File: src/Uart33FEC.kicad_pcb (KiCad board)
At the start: 2 copper layers, 24 x 27.9 mm, 28 parts, among them J1 105444-0001, J2 B4B-XH-A, Q1 DMP3099L-13, U1 FT230XS, U2 MIC2005A-1

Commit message: Changed pinout to GND RXD TXD 3V3
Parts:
- moved D1 1.31 mm to (32.0, 39.2)
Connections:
- J2 pad 1: RX -> GND
- J2 pad 2: GND -> RX
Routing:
- net GND: track 110.2 -> 112.3 mm
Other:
- board text added: "Uart33FEC BXXXX"
- board text removed: "Uart33FEC AXXXX"
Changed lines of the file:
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@@
 			(chamfer_ratio 0.2)
 			(chamfer top_left bottom_left)
-			(net 17 "RX")
+			(net 1 "GND")
 		)
 		(pad "2" smd roundrect
@@
 			(layers "F.Cu" "F.Paste" "F.Mask")
 			(roundrect_rratio 0.25)
-			(net 1 "GND")
+			(net 17 "RX")
 		)
 		(pad "3" smd roundrect
@@
 		)
 		(property "Value" "10uF"
-			(at 0 1.7 0)
+			(at 1 1.6 0)
 			(layer "B.SilkS")
 			(effects
@@
 	(footprint "Medo64:D TVS SM05T1G (SOT23-3)"
 		(layer "B.Cu")
-		(at 30.75 39.6 180)
+		(at 32 39.2 180)
 		(descr "SM05T1G [SM05T1GOSCT-ND]")
 		(property "Reference" "D1"
-			(at -2.25 0 0)
+			(at 0 -1 0)
 			(layer "B.SilkS")
 			(effects
@@
 	)
 	(gr_text "RX"
-		(at 28.25 38.7 0)
+		(at 30.8 38.7 0)
 		(layer "F.SilkS" knockout)
 		(effects
@@
 	)
 	(gr_text "TX"
-		(at 33.2 38.7 0)
+		(at 33.1 38.7 0)
 		(layer "F.SilkS" knockout)
 		(effects
@@
 		)
 	)
-	(gr_text "Uart33FEC AXXXX"
+	(gr_text "Uart33FEC BXXXX"
 		(at 21 33 90)
 		(layer "F.SilkS")
@@
 	)
 	(gr_text "GND"
-		(at 30.75 38.7 0)
+		(at 28.1 38.7 0)
 		(layer "F.SilkS" knockout)
 		(effects
@@
 	)
 	(segment
+		(start 28.25 40.8)
+		(end 28.25 38.8)
+		(width 0.35)
+		(layer "F.Cu")
+		(net 1)
+	)
+	(segment
 		(start 33.6325 30.6825)
 		(end 34.7 30.6825)
@@
 	)
 	(via
-		(at 30.75 40.8)
+		(at 29.4 23.2)
 		(size 0.6)
 		(drill 0.3)
@@
 	)
 	(via
-		(at 29.4 23.2)
+		(at 28.25 38.8)
 		(size 0.6)
 		(drill 0.3)
@@
 	)
 	(segment
-		(start 30.75 38.85)
-		(end 30.75 40.8)
-		(width 0.35)
-		(layer "B.Cu")
-		(net 1)
-	)
-	(segment
 		(start 36.4 30.25)
 		(end 34.9 30.25)
@@
 	)
 	(segment
-		(start 30.75 37.6)
-		(end 28.75 37.6)
+		(start 28.25 38.275)
+		(end 28.3 38.225)
 		(width 0.35)
 		(layer "B.Cu")
@@
 	)
 	(segment
-		(start 30.75 37.9)
-		(end 30.75 37.6)
+		(start 27.925 38.225)
+		(end 27.5 37.8)
 		(width 0.35)
 		(layer "B.Cu")
@@
 	)
 	(segment
-		(start 30.75 38.625)
-		(end 30.75 37.9)
+		(start 33.075 38.225)
+		(end 33.4 37.9)
 		(width 0.35)
 		(layer "B.Cu")
@@
 	)
 	(segment
-		(start 30.75 37.6)
-		(end 32.1 37.6)
+		(start 33.9 33.3)
+		(end 33.9 35.05)
 		(width 0.35)
 		(layer "B.Cu")
@@
 	)
 	(segment
-		(start 33.9 33.3)
-		(end 33.9 35.05)
+		(start 37.8 35.05)
+		(end 36.7 35.05)
 		(width 0.35)
 		(layer "B.Cu")
@@
 	)
 	(segment
-		(start 37.8 35.05)
-		(end 36.7 35.05)
+		(start 33.4 37.9)
+		(end 33.4 36.3)
 		(width 0.35)
 		(layer "B.Cu")
@@
 	)
 	(segment
+		(start 27.5 36.2)
+		(end 27.5 37.8)
+		(width 0.35)
+		(layer "B.Cu")
+		(net 1)
+	)
+	(segment
 		(start 30.05 23.85)
 		(end 33.95 23.85)
@@
 	)
 	(segment
-		(start 28.75 37.6)
-		(end 27.5 36.35)
-		(width 0.35)
-		(layer "B.Cu")
-		(net 1)
-	)
-	(segment
 		(start 29.25 23.05)
 		(end 29.25 22.1)
@@
 	)
 	(segment
+		(start 32 38.225)
+		(end 28.3 38.225)
+		(width 0.35)
+		(layer "B.Cu")
+		(net 1)
+	)
+	(segment
 		(start 33.9 35.05)
 		(end 33.9 35.7)
@@
 	)
 	(segment
+		(start 28.25 38.8)
+		(end 28.25 38.275)
+		(width 0.35)
+		(layer "B.Cu")
+		(net 1)
+	)
+	(segment
 		(start 36.7 35.05)
 		(end 36.7 34.75)
@@
 	)
 	(segment
+		(start 28.3 38.225)
+		(end 27.925 38.225)
+		(width 0.35)
+		(layer "B.Cu")
+		(net 1)
+	)
+	(segment
 		(start 29.4 23.2)
 		(end 29.25 23.05)
@@
 	)
 	(segment
-		(start 32.1 37.6)
-		(end 33.4 36.3)
-		(width 0.35)
-		(layer "B.Cu")
-		(net 1)
-	)
-	(segment
 		(start 33.9 35.7)
 		(end 33.4 36.2)
@@
 	)
 	(segment
+		(start 32 38.225)
+		(end 33.075 38.225)
+		(width 0.35)
+		(layer "B.Cu")
+		(net 1)
+	)
+	(segment
 		(start 31.25 23.65)
 		(end 30.7 24.2)
@@
 	)
 	(segment
-		(start 29.3 37.9)
-		(end 26.5 37.9)
-		(width 0.2)
-		(layer "F.Cu")
-		(net 9)
-	)
-	(segment
-		(start 26.5 37.9)
-		(end 24.55 39.85)
+		(start 24.55 39.85)
+		(end 24.55 42.65)
 		(width 0.2)
 		(layer "F.Cu")
@@
 	)
 	(segment
-		(start 24.55 39.85)
-		(end 24.55 42.65)
-		(width 0.2)
-		(layer "F.Cu")
-		(net 9)
-	)
-	(segment
 		(start 39.45 37.9)
 		(end 29.3 37.9)
@@
 	)
 	(segment
+		(start 26.5 37.9)
+		(end 24.55 39.85)
+		(width 0.2)
+		(layer "F.Cu")
+		(net 9)
+	)
+	(segment
 		(start 42.5 35.7)
 		(end 42.5 31.3)
@@
 		(net 9)
 	)
+	(segment
+		(start 29.3 37.9)
+		(end 26.5 37.9)
+		(width 0.2)
+		(layer "F.Cu")
+		(net 9)
+	)
 	(via
 		(at 24.55 42.65)
@@
 	)
 	(segment
-		(start 29.199944 40.8)
-		(end 29.2 40.800056)
-		(width 0.2)
-		(layer "F.Cu")
-		(net 17)
-	)
-	(segment
-		(start 28.25 40.8)
-		(end 29.199944 40.8)
-		(width 0.35)
-		(layer "F.Cu")
-		(net 17)
-	)
-	(segment
 		(start 29.2825 30.7)
 		(end 26.1 30.7)
@@
 	)
 	(via
-		(at 29.2 40.800056)
+		(at 30.75 40.8)
 		(size 0.6)
 		(drill 0.3)
@@
 	)
 	(segment
-		(start 29.2 40.800056)
-		(end 29.799944 40.800056)
+		(start 26.05 38.25)
+		(end 26.05 30.65)
 		(width 0.35)
 		(layer "B.Cu")
@@
 	)
 	(segment
-		(start 29.8 40.574998)
-		(end 25.65 36.424998)
+		(start 28.6 40.8)
+		(end 26.05 38.25)
 		(width 0.35)
 		(layer "B.Cu")
@@
 	)
 	(segment
-		(start 25.65 31.05)
-		(end 26.05 30.65)
+		(start 30.75 40.8)
+		(end 28.6 40.8)
 		(width 0.35)
 		(layer "B.Cu")
@@
 	)
 	(segment
-		(start 25.65 36.424998)
-		(end 25.65 31.05)
+		(start 30.75 40.8)
+		(end 30.749944 40.800056)
 		(width 0.35)
 		(layer "B.Cu")
@@
 	(segment
 		(start 33.25 40.8)
-		(end 32.3 40.8)
+		(end 33.250022 40.8)
 		(width 0.35)
 		(layer "F.Cu")
@@
 	)
 	(via
-		(at 32.3 40.8)
+		(at 33.250022 40.8)
 		(size 0.6)
 		(drill 0.3)
@@
 	)
 	(segment
-		(start 24.35 38.05)
-		(end 24.35 30.1)
+		(start 31.850022 42.2)
+		(end 33.250022 40.8)
 		(width 0.35)
 		(layer "B.Cu")
@@
 	)
 	(segment
-		(start 30.8 42.25)
-		(end 28.55 42.25)
+		(start 25.63932 28.76068)
+		(end 24.35 30.05)
 		(width 0.35)
 		(layer "B.Cu")
@@
 	)
 	(segment
-		(start 31.7 41.35)
-		(end 30.8 42.25)
+		(start 24.35 38.85)
+		(end 27.7 42.2)
 		(width 0.35)
 		(layer "B.Cu")
@@
 	)
 	(segment
-		(start 28.55 42.25)
-		(end 24.35 38.05)
+		(start 26.050002 28.76068)
+		(end 25.63932 28.76068)
 		(width 0.35)
 		(layer "B.Cu")
@@
 	)
 	(segment
-		(start 31.7 40.575)
-		(end 31.7 41.35)
+		(start 27.7 42.2)
+		(end 31.850022 42.2)
 		(width 0.35)
 		(layer "B.Cu")
@@
 	)
 	(segment
-		(start 31.925 40.8)
-		(end 31.7 40.575)
-		(width 0.35)
-		(layer "B.Cu")
-		(net 18)
-	)
-	(segment
-		(start 32.3 40.8)
-		(end 31.925 40.8)
-		(width 0.35)
-		(layer "B.Cu")
-		(net 18)
-	)
-	(segment
-		(start 24.35 30.1)
-		(end 25.68932 28.76068)
-		(width 0.35)
-		(layer "B.Cu")
-		(net 18)
-	)
-	(segment
-		(start 25.68932 28.76068)
-		(end 26.050002 28.76068)
+		(start 24.35 30.05)
+		(end 24.35 38.85)
 		(width 0.35)
 		(layer "B.Cu")

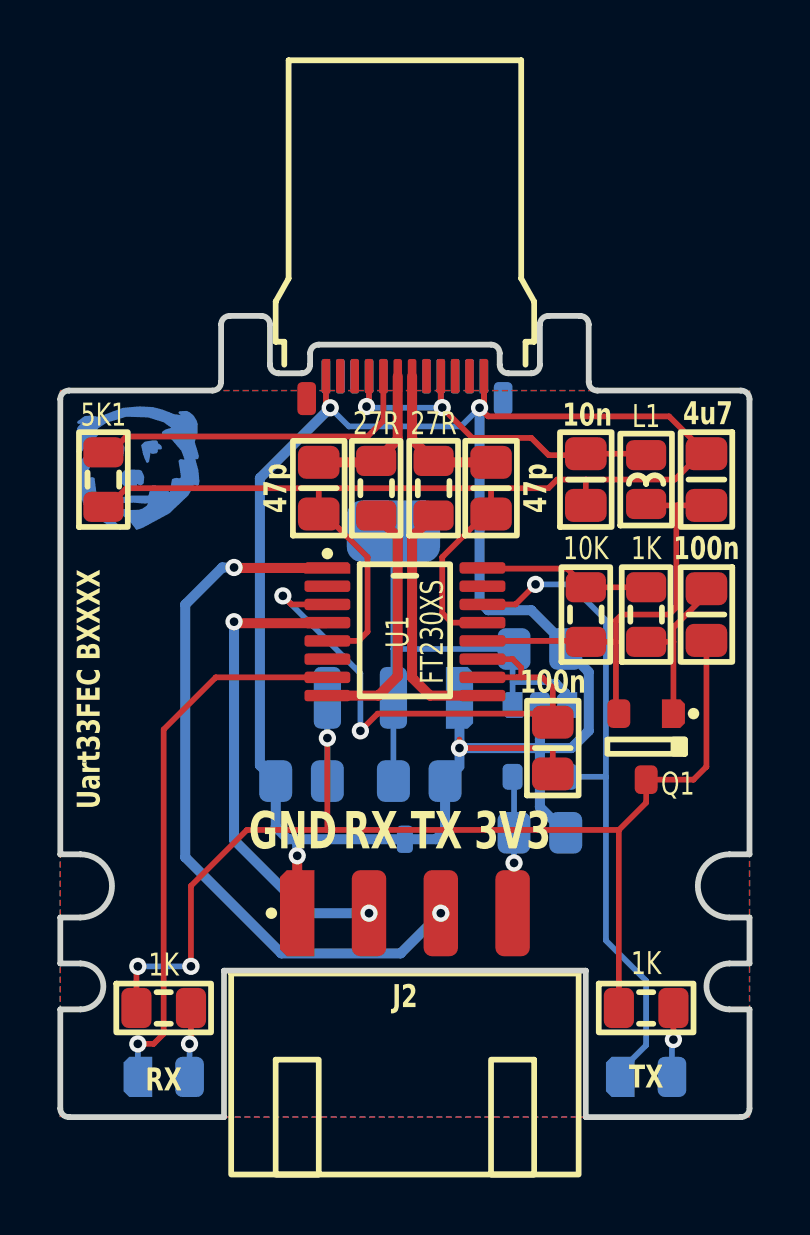
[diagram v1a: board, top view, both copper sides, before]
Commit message: Changed load switch (400mA limit)
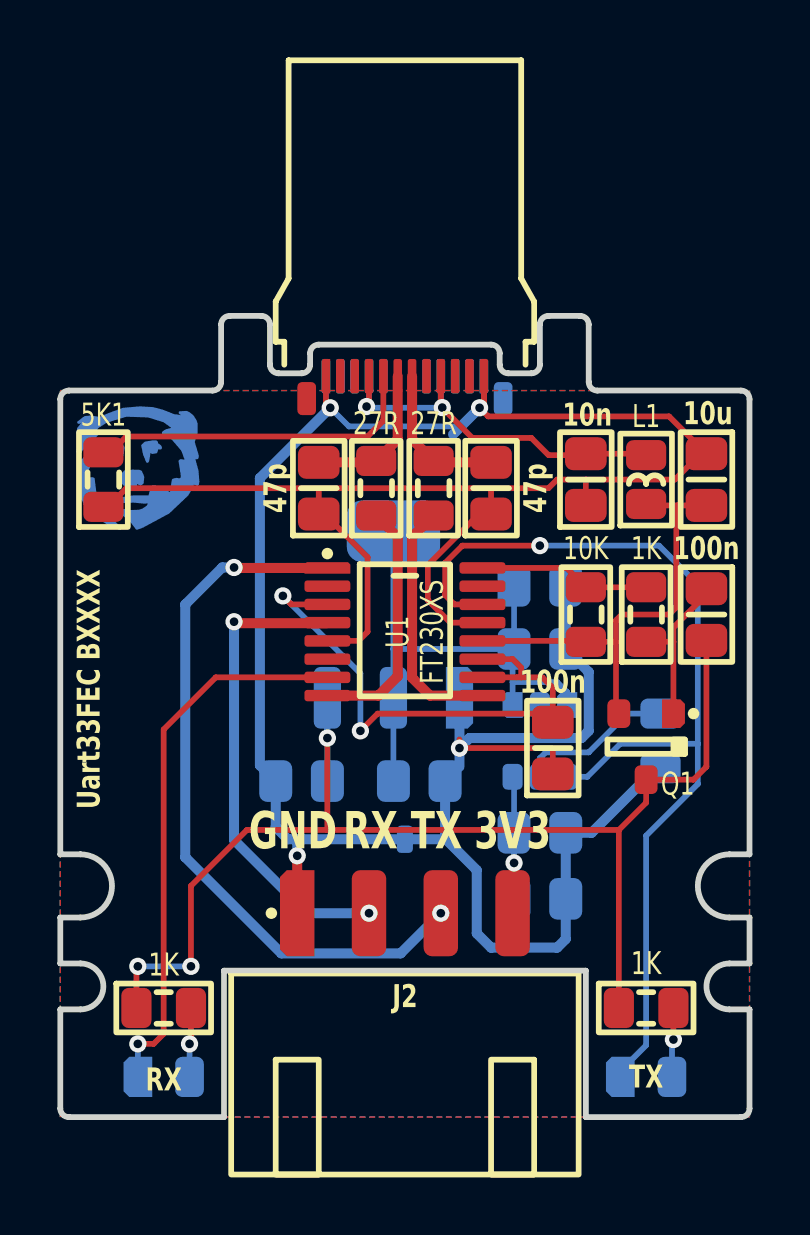
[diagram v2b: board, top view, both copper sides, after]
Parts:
- added C12: 10uF, Medo64:C (0805), B.Cu at (36.7, 40.3)
- added C8: 10u, Medo64:C (0805), B.Cu at (36.7, 29.4)
- added R8: 75K, Medo64:R (0805), B.Cu at (40.9, 34.8)
- C6: renamed from C8; value 10uF -> 100n
- C7: renamed from C6; value 1uF -> 100n
- C9: renamed from C7; value 4u7 -> 10u
- U2: value MIC2005A-1 -> AP22652; footprint Medo64:U LoadSwitch 500mA [MIC2005A-1] (SOT23-5) -> Medo64:U LoadSwitch Adjustable [AP22653AW6-7] (SOT23-6)
- renumbered C9 to C10, C10 to C11
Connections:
- U2 pad 5: Vout -> ILIM
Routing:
- net LED_TX: track 23.0 -> 35.1 mm
- net ILIM: track 0.00 -> 5.49 mm
- net GND: track 112.3 -> 117.6 mm
- net Vout: track 4.72 -> 7.02 mm
- net 3V3out: track 17.3 -> 19.5 mm

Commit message: Refactored output handling
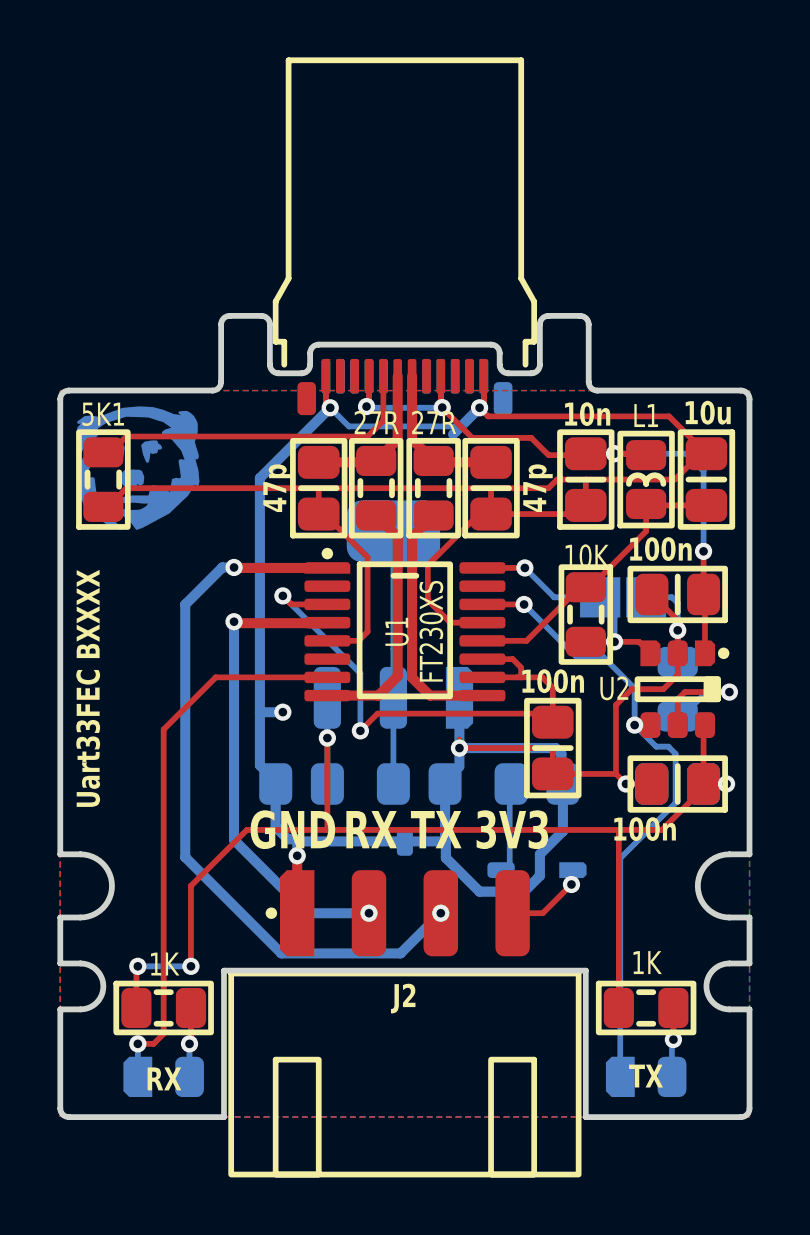
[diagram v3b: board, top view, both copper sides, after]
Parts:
- removed the C4 at (42.5, 30.4)
- removed Q1: DMP3099L-13, Medo64:Q MOSFET-P (SOT23-3)
- removed the R5 at (40.4, 30.4)
- added D1: CUS08F30, Medo64:D (SOD323), B.Cu at (36.6, 39.3)
- added JP1: ALWAYS ON, Medo64:JP (0805), B.Cu at (39.6, 29.8)
- C10: renamed from C11; value 10uF -> 10u
- C11: renamed from C12; value 10uF -> 10u
- C5: renamed from C7; moved to F.Cu
- C6: moved to F.Cu
- C9: renamed from C10; value 10uF -> 10u
- D2: renamed from D1; footprint Medo64:D TVS SM05T1G (SOT23-3) -> Medo64:D TVS 3.3V [D1213A-02SOL-7] (SOT23-3)
- R7: renamed from R8; value 75K -> 100K
- U2: footprint Medo64:U LoadSwitch Adjustable [AP22653AW6-7] (SOT23-6) -> Medo64:U LoadSwitch Adjustable [AP22652W6-7] (SOT23-6); moved to F.Cu
- moved C8 8.41 mm to (41.5, 36.3), turned to 180 degrees
- moved C5 5.16 mm to (41.5, 29.7), turned to 180 degrees
- moved U2 5.13 mm to (41.5, 33.0)
- moved C6 5.09 mm to (41.5, 36.3), turned to 180 degrees
- moved C11 4.00 mm to (36.6, 36.3)
- moved R7 1.90 mm to (41.5, 33.0), turned to 90 degrees
- moved C10 0.10 mm to (32.5, 36.3)
- moved C9 0.10 mm to (28.4, 36.3)
- moved D2 0.10 mm to (32.0, 39.3)
- turned R6 to -90 degrees
- renumbered C5 to C4, C9 to C7, R6 to R5, R7 to R6
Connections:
- C10 pad 1: 3V3out -> 3V3_SWITCHED
- C11 pad 1: Vout -> OUT_3V3
- C3 pad 2: USB_V+ -> USB_5V
- C5 pad 1: 3V3out -> USB_5V
- C6 pad 1: Vout -> 5V_SWITCHED
- C8 pad 1: 3V3out -> 5V_SWITCHED
- J1 pad A4: USB_V+ -> USB_5V
- J1 pad A9: USB_V+ -> USB_5V
- J1 pad B04: USB_V+ -> USB_5V
- J1 pad B09: USB_V+ -> USB_5V
- J2 pad 4: Vout -> OUT_3V3_PROT
- L1 pad 2: USB_V+ -> USB_5V
- U2 pad 1: 3V3out -> USB_5V
- U2 pad 3: 3V3out -> PWREN#
- U2 pad 6: Vout -> 5V_SWITCHED
- VR1 pad 2: 3V3out -> 3V3_SWITCHED
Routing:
- net USB_5V: track 0.00 -> 24.4 mm, vias 0 -> 4
- net 3V3out: track 19.5 -> 0.00 mm
- net USB_V+: track 14.7 -> 0.00 mm, vias 2 -> 0
- net LED_TX: track 35.1 -> 22.2 mm, vias 1 -> 2
- net 3V3_SWITCHED: track 0.00 -> 8.70 mm
- net Vout: track 7.02 -> 0.00 mm, vias 1 -> 0
- net GND: track 117.6 -> 124.0 mm, vias 4 -> 7
- net PWREN#': track 5.58 -> 0.00 mm
- net 5V: track 15.7 -> 10.3 mm
- net OUT_3V3_PROT: track 0.00 -> 3.01 mm, vias 0 -> 1
- net OUT_3V3: track 0.00 -> 2.90 mm
- net PWREN#: track 5.98 -> 8.70 mm, vias 0 -> 2
- net 5V_SWITCHED: track 44.4 -> 43.5 mm, vias 3 -> 4
- net ILIM: track 5.49 -> 4.81 mm, vias 0 -> 1

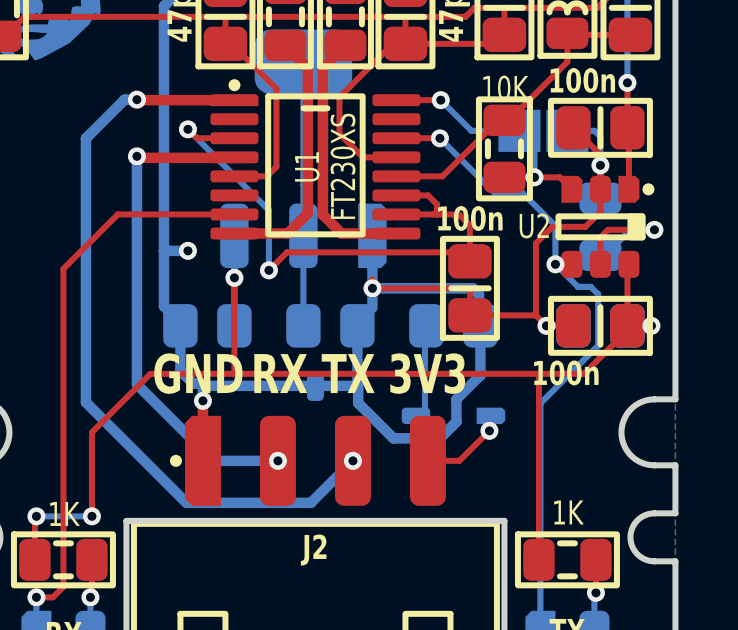
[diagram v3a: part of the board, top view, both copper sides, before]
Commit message: Connected 3V3 output lines
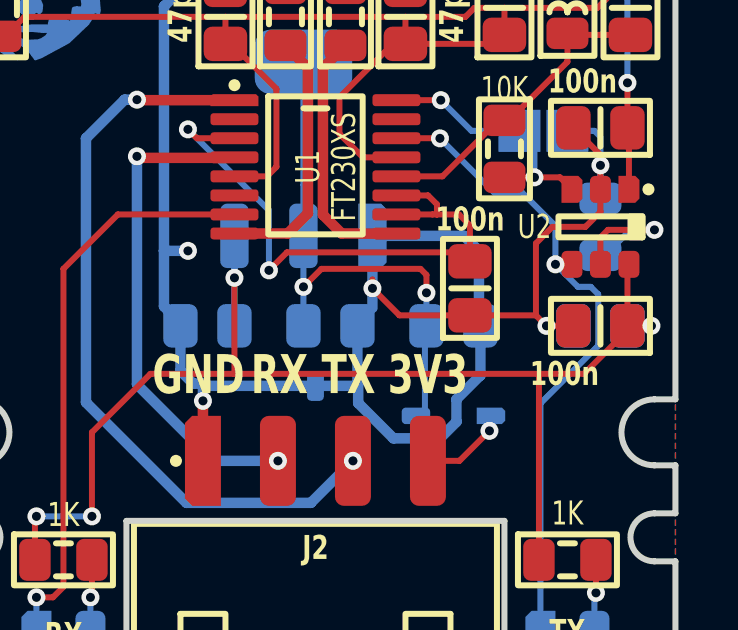
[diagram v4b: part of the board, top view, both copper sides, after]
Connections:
- net OUT_3V3_PROT renamed 3V3_OUT
- net USB_5V renamed 5V_USB
- C11 pad 1: OUT_3V3 -> 3V3_SWITCHED
- D1 pad 2: OUT_3V3 -> 3V3_SWITCHED
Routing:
- net 3V3_SWITCHED: track 8.70 -> 17.8 mm, vias 0 -> 2
- net OUT_3V3: track 2.90 -> 0.00 mm
- net GND: track 124.0 -> 125.4 mm
